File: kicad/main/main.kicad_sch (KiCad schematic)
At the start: 15 parts, among them J3 Conn_01x07_Pin, J4 Conn_01x04_Pin, P1 USB_C_Plug_USB2.0, SW3 SW_Push, SW4 SW_Push, U1 HUSB237

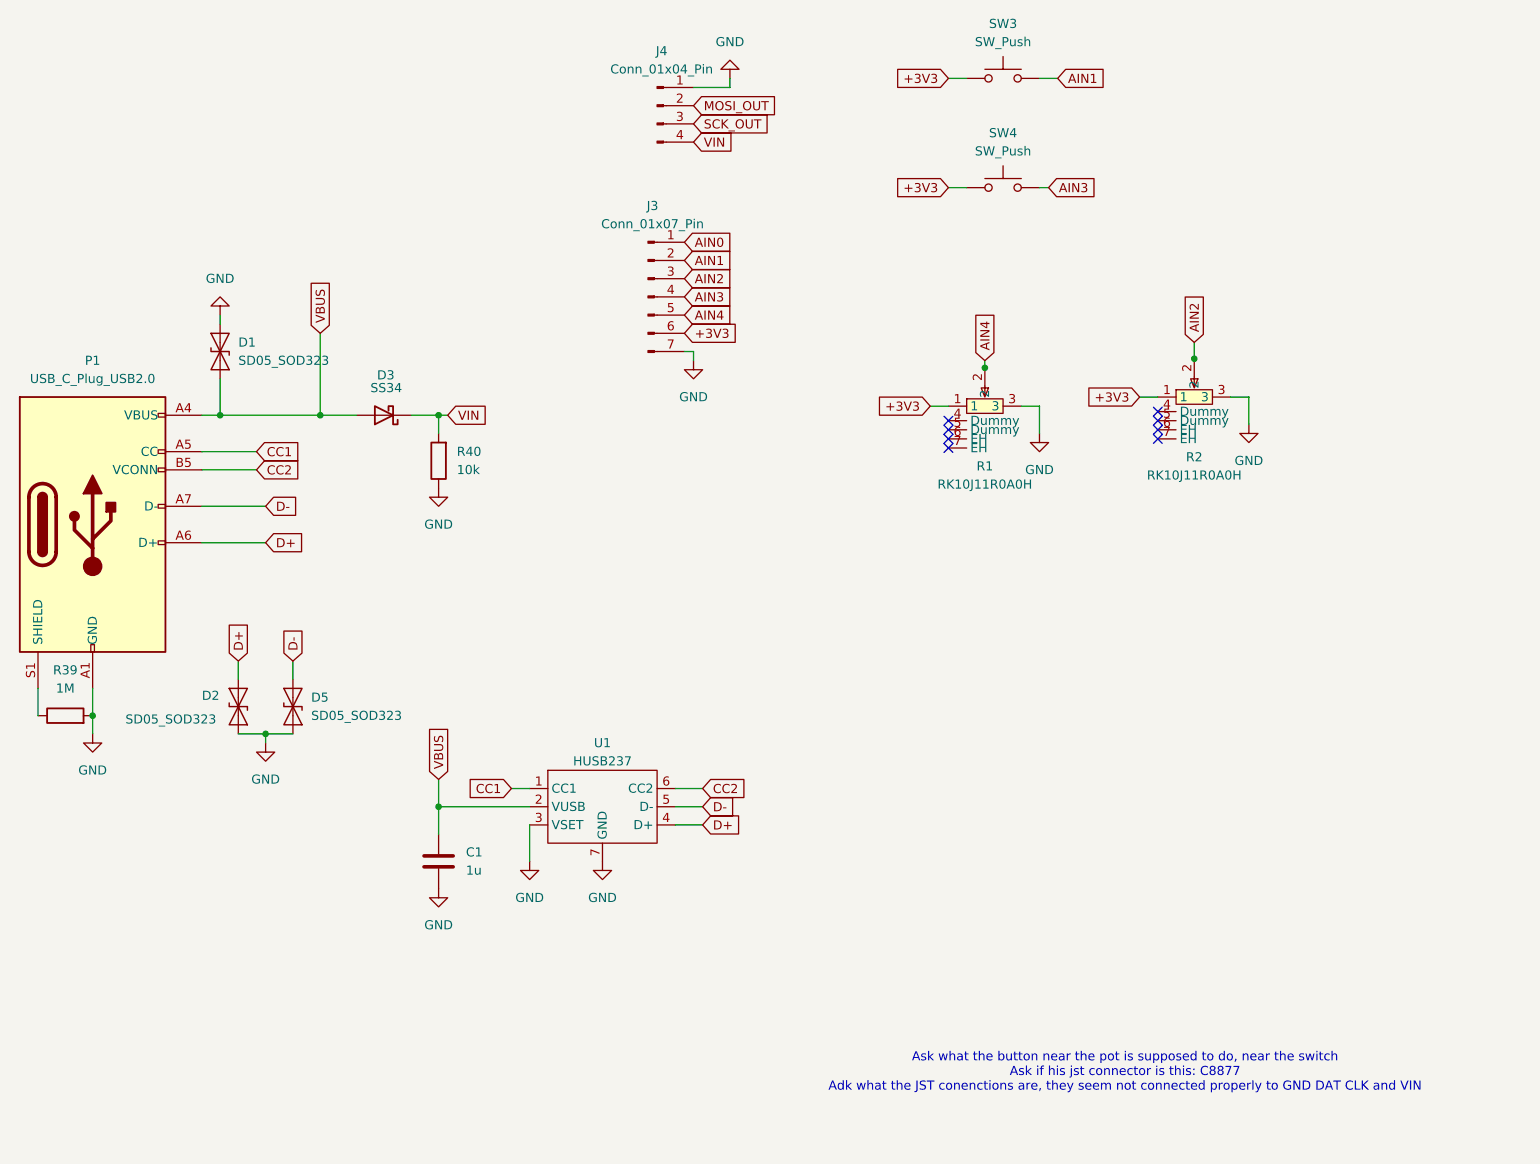
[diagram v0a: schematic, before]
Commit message: Switches added
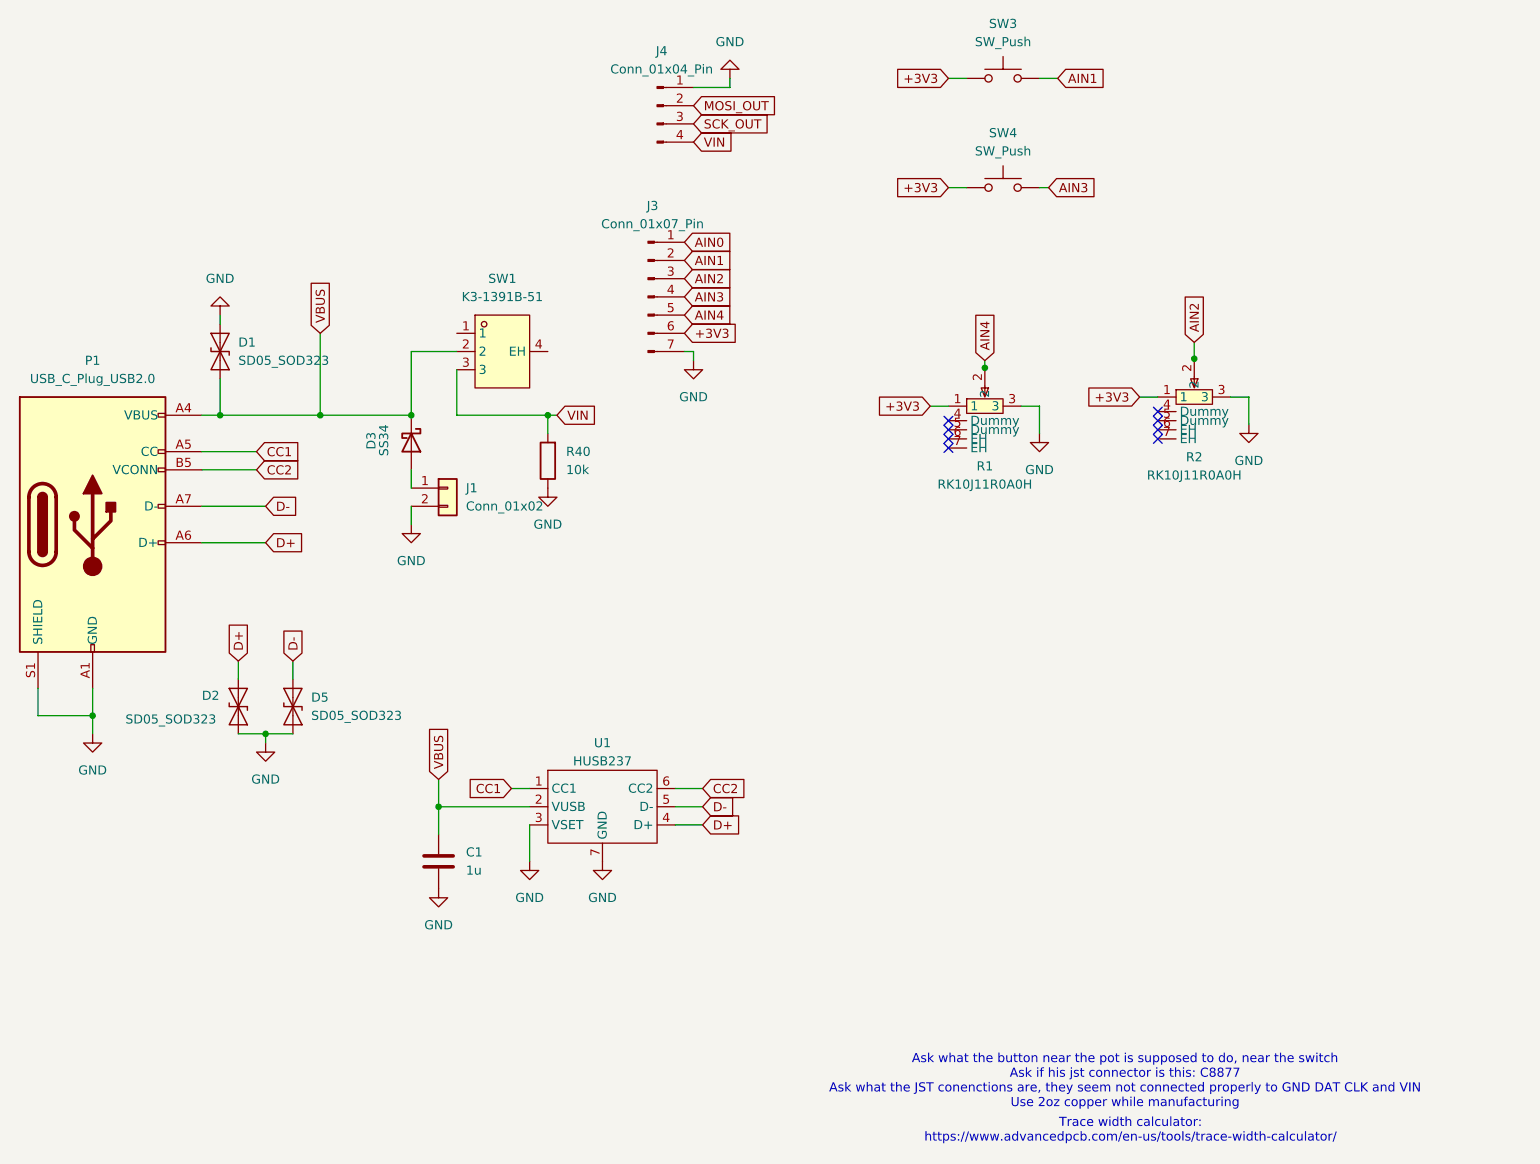
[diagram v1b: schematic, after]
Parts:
- removed R39: 1M, Resistor_SMD:R_0603_1608Metric_Pad0.98x0.95mm_HandSolder, symbol Device:R
- added J1: Conn_01x02, symbol Connector_Generic:Conn_01x02
- added SW1: K3-1391B-51, easyeda2kicad:SW-TH_K3-1391B-51, symbol easyeda2kicad:K3-1391B-51
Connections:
- net GND: now also P1.S1 (SHIELD), J1.2 (Pin_2)
- net VBUS: now also D3.1 (K), SW1.2; no longer D3.2 (A)
- net VIN: now also SW1.3; no longer D3.1 (K)
- new net: D3.2 (A), J1.1 (Pin_1)
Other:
- note added: "Ask what the button near the pot is supposed to do, near the switch Ask if his jst connector is this: C8877 Ask what the JST conenctions are, they seem not connected properly to GND DAT CLK and VIN Use 2oz copper while manufacturing"
- note added: "Trace width calculator: https://www.advancedpcb.com/en-us/tools/trace-width-calculator/"
- note removed: "Ask what the button near the pot is supposed to do, near the switch Ask if his jst connector is this: C8877 Adk what the JST conenctions are, they seem not connected properly to GND DAT CLK and VIN"
- moved on the sheet: D3, R40

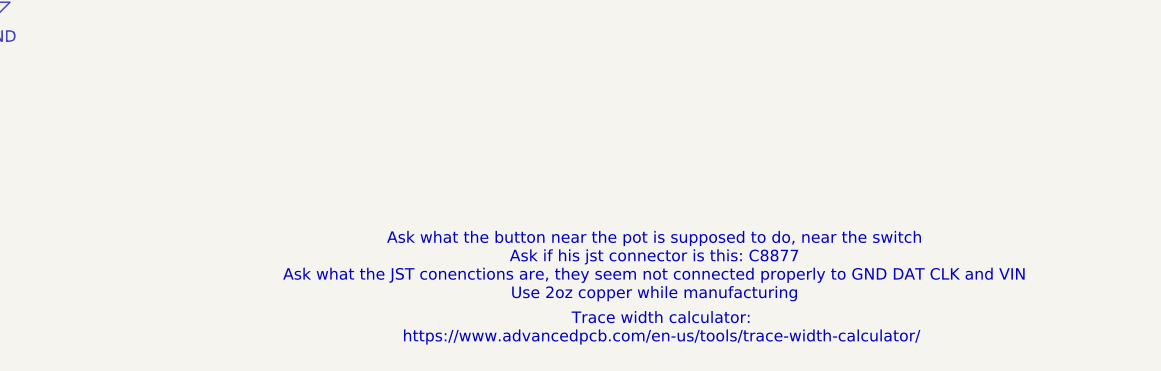
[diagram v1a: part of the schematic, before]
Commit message: Added extra switched
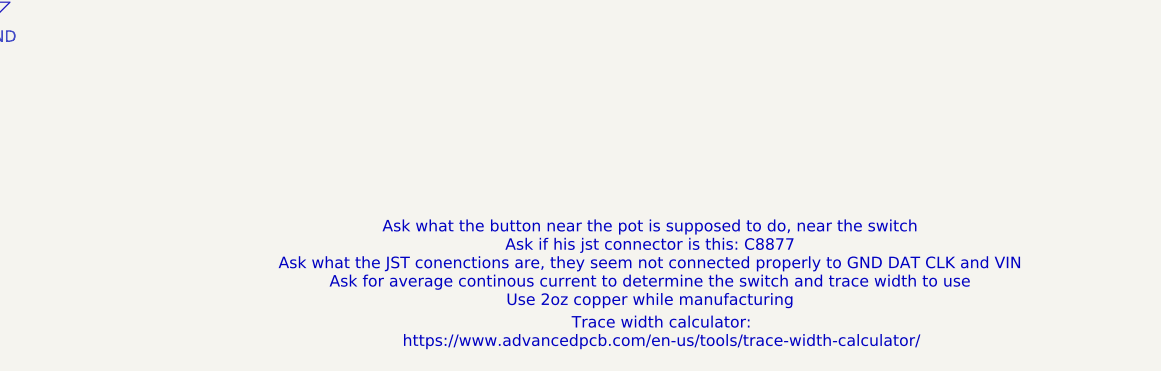
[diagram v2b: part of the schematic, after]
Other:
- note added: "Ask what the button near the pot is supposed to do, near the switch Ask if his jst connector is this: C8877 Ask what the JST conenctions are, they seem not connected properly to GND DAT CLK and VIN Ask for average continous current to determine the switch and trace width to use Use 2oz copper while manufacturing"
- note removed: "Ask what the button near the pot is supposed to do, near the switch Ask if his jst connector is this: C8877 Ask what the JST conenctions are, they seem not connected properly to GND DAT CLK and VIN Use 2oz copper while manufacturing"
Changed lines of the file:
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@@
 	(text "Trace width calculator:\nhttps://www.advancedpcb.com/en-us/tools/trace-width-calculator/"
 		(exclude_from_sim no)
-		(at 231.14 178.562 0)
+		(at 231.14 179.07 0)
 		(effects
 			(font
@@
 		)
 	)
-	(text "Ask what the button near the pot is supposed to do, near the switch\nAsk if his jst connector is this: C8877\nAsk what the JST conenctions are, they seem not connected properly to GND DAT CLK and VIN\nUse 2oz copper while manufacturing"
+	(text "Ask what the button near the pot is supposed to do, near the switch\nAsk if his jst connector is this: C8877\nAsk what the JST conenctions are, they seem not connected properly to GND DAT CLK and VIN\nAsk for average continous current to determine the switch and trace width to use\nUse 2oz copper while manufacturing"
 		(exclude_from_sim yes)
-		(at 230.378 171.704 0)
+		(at 229.87 171.45 0)
 		(effects
 			(font

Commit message: Finished design
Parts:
- removed SW1: K3-1391B-51, easyeda2kicad:SW-TH_K3-1391B-51, symbol easyeda2kicad:K3-1391B-51
- added SW1: MK-12C03-G015, easyeda2kicad:SW-SMD_MK-12C03-G015, symbol easyeda2kicad:MK-12C03-G015
- added U2: ZX-PH2.0-WT4P, easyeda2kicad:CONN-SMD_4P-P2.00_C2001RS10411M0101RC, symbol easyeda2kicad:ZX-PH2.0-WT4P
- C1: footprint (none) -> Capacitor_SMD:C_0805_2012Metric
- J2: renamed from J1; footprint (none) -> Connector_PinHeader_2.54mm:PinHeader_1x02_P2.54mm_Vertical
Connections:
- net GND: now also U2.3, U2.5, U2.6
- net MOSI_OUT: now also U2.2
- net SCK_OUT: now also U2.1
- net VBUS: now also SW1.3
- net VIN: now also SW1.2, U2.4
- no-connect marks 8 -> 13

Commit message: Rewired PCB
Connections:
- net D+: now also D2.1 (A1); no longer D2.2 (A2)
- net D-: now also D5.1 (A1); no longer D5.2 (A2)
- net GND: now also D2.2 (A2), D5.2 (A2); no longer D2.1 (A1), D5.1 (A1)
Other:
- moved on the sheet: C1, D1, D2, D3, D5, J2, J3, J4, P1, R1, R2, R40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

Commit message: Rewired PCB
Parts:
- removed D3: SS34, Diode_SMD:D_SMA, symbol Diode:SS34
- added D3: 1N4007, Diode_THT:D_DO-41_SOD81_P10.16mm_Horizontal, symbol Diode:1N4007
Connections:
- net VBUS: now also D3.1 (K)
- net at J2.1 (Pin_1): now also D3.2 (A)
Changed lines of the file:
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@@
 	)
 	(symbol
-		(lib_id "Diode:SS34")
+		(lib_id "Diode:1N4007")
 		(at 132.08 93.98 270)
 		(unit 1)
@@
 		(on_board yes)
 		(dnp no)
+		(fields_autoplaced yes)
 		(property "Reference" "D3"
-			(at 126.492 93.726 0)
+			(at 134.62 92.7099 90)
 			(effects
 				(font
 					(size 1.27 1.27)
 				)
+				(justify left)
 			)
 		)
-		(property "Value" "SS34"
-			(at 128.27 93.6625 0)
+		(property "Value" "1N4007"
+			(at 134.62 95.2499 90)
 			(effects
 				(font
 					(size 1.27 1.27)
 				)
+				(justify left)
 			)
 		)
-		(property "Footprint" "Diode_SMD:D_SMA"
+		(property "Footprint" "Diode_THT:D_DO-41_SOD81_P10.16mm_Horizontal"
 			(at 127.635 93.98 0)
 			(effects
@@
 			)
 		)
-		(property "Datasheet" "https://www.vishay.com/docs/88751/ss32.pdf"
+		(property "Datasheet" "http://www.vishay.com/docs/88503/1n4001.pdf"
 			(at 132.08 93.98 0)
 			(effects
@@
 			)
 		)
-		(property "Description" "40V 3A Schottky Diode, SMA"
+		(property "Description" "1000V 1A General Purpose Rectifier Diode, DO-41"
 			(at 132.08 93.98 0)
 			(effects
@@
 			)
 		)
-		(property "LCSC Part" "C8678"
+		(property "Sim.Device" "D"
 			(at 132.08 93.98 0)
 			(effects
@@
 			)
 		)
-		(pin "1"
+		(property "Sim.Pins" "1=K 2=A"
+			(at 132.08 93.98 0)
+			(effects
+				(font
+					(size 1.27 1.27)
+				)
+				(hide yes)
+			)
 		)
 		(pin "2"
 		)
+		(pin "1"
+		)
 		(instances

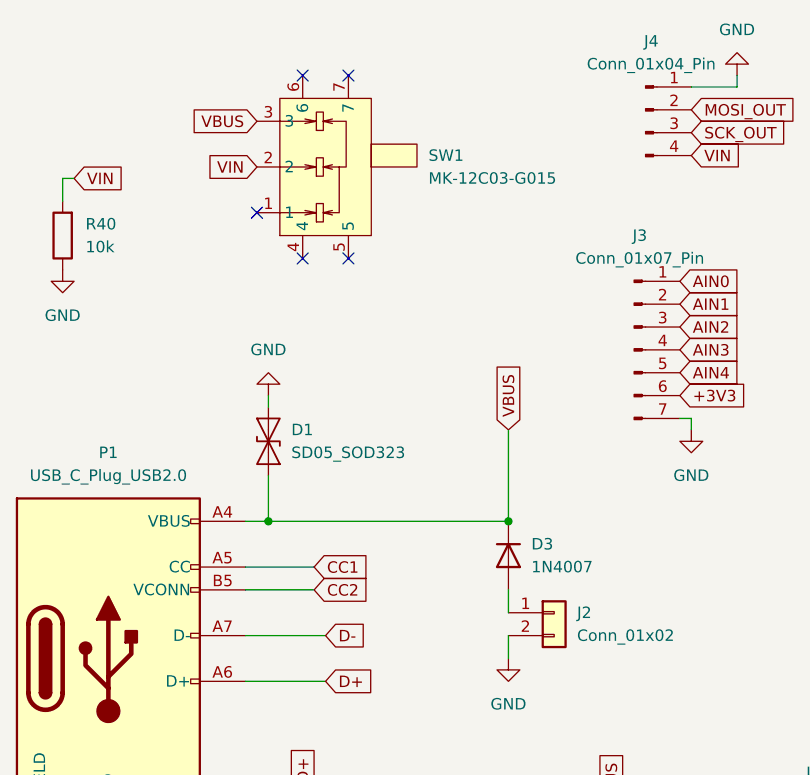
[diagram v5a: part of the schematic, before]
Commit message: Final push with moved components
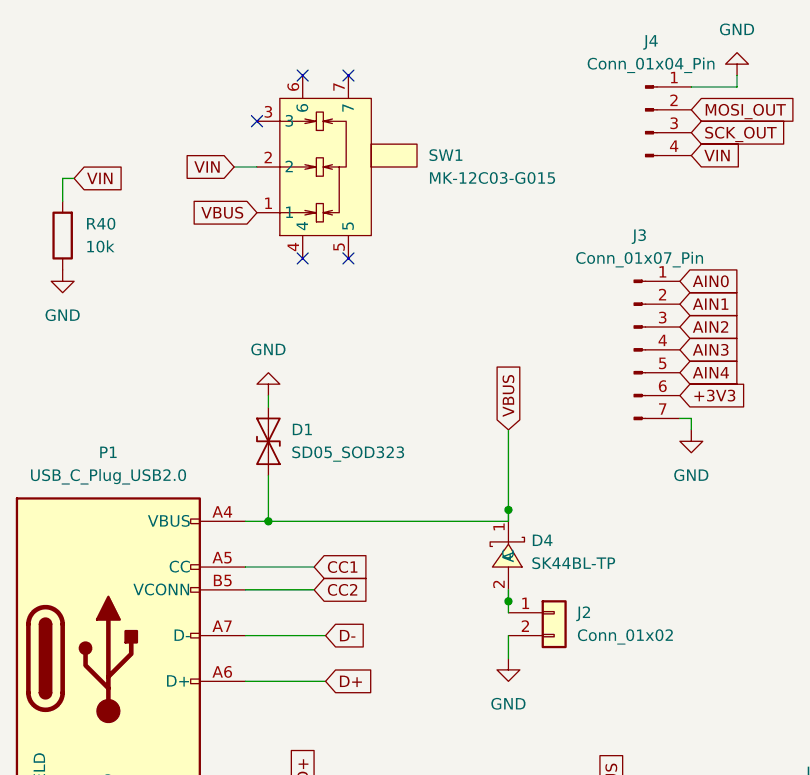
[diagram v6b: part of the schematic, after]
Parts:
- removed D3: 1N4007, Diode_THT:D_DO-41_SOD81_P10.16mm_Horizontal, symbol Diode:1N4007
- added D4: SK44BL-TP, easyeda2kicad:SMB_L4.6-W3.6-LS5.3-RD, symbol easyeda2kicad:SK44BL-TP
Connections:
- net VBUS: now also SW1.1, D4.1 (C); no longer SW1.3
- net at J2.1 (Pin_1): now also D4.2 (A)
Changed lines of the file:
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@@
 	)
 	(junction
-		(at 132.08 90.17)
+		(at 111.76 134.62)
 		(diameter 0)
 		(color 0 0 0 0)
 	)
 	(junction
-		(at 111.76 134.62)
+		(at 132.08 88.9)
 		(diameter 0)
 		(color 0 0 0 0)
@@
 		(color 0 0 0 0)
 	)
+	(junction
+		(at 132.08 99.06)
+		(diameter 0)
+		(color 0 0 0 0)
+	)
 	(no_connect
 		(at 213.36 101.09)
 	)
 	(no_connect
-		(at 104.14 55.88)
+		(at 104.14 45.72)
 	)
 	(no_connect
@@
 	(wire
 		(pts
-			(xy 132.08 97.79) (xy 132.08 100.33)
+			(xy 132.08 97.79) (xy 132.08 99.06)
 		)
 		(stroke
@@
 	(wire
 		(pts
-			(xy 132.08 80.01) (xy 132.08 90.17)
+			(xy 132.08 80.01) (xy 132.08 88.9)
+		)
+		(stroke
+			(width 0)
+			(type default)
+		)
+	)
+	(wire
+		(pts
+			(xy 132.08 99.06) (xy 132.08 100.33)
 		)
 		(stroke
@@
 	(wire
 		(pts
+			(xy 101.6 50.8) (xy 104.14 50.8)
+		)
+		(stroke
+			(width 0)
+			(type default)
+		)
+	)
+	(wire
+		(pts
 			(xy 102.87 107.95) (xy 111.76 107.95)
 		)
@@
 	(wire
 		(pts
+			(xy 132.08 88.9) (xy 132.08 90.17)
+		)
+		(stroke
+			(width 0)
+			(type default)
+		)
+	)
+	(wire
+		(pts
 			(xy 176.53 124.46) (xy 180.34 124.46)
 		)
@@
 	(global_label "VIN"
 		(shape input)
-		(at 104.14 50.8 180)
+		(at 101.6 50.8 180)
 		(fields_autoplaced yes)
 		(effects
@@
 		)
 		(property "Intersheetrefs" "${INTERSHEET_REFS}"
-			(at 98.1309 50.8 0)
+			(at 95.5909 50.8 0)
 			(effects
 				(font
@@
 	(global_label "VBUS"
 		(shape input)
-		(at 104.14 45.72 180)
+		(at 104.14 55.88 180)
 		(fields_autoplaced yes)
 		(effects
@@
 		)
 		(property "Intersheetrefs" "${INTERSHEET_REFS}"
-			(at 96.2562 45.72 0)
+			(at 96.2562 55.88 0)
 			(effects
 				(font
@@
 	)
 	(symbol
-		(lib_id "Diode:1N4007")
-		(at 132.08 93.98 270)
-		(unit 1)
-		(exclude_from_sim no)
-		(in_bom yes)
-		(on_board yes)
-		(dnp no)
-		(fields_autoplaced yes)
-		(property "Reference" "D3"
-			(at 134.62 92.7099 90)
-			(effects
-				(font
-					(size 1.27 1.27)
-				)
-				(justify left)
-			)
-		)
-		(property "Value" "1N4007"
-			(at 134.62 95.2499 90)
-			(effects
-				(font
-					(size 1.27 1.27)
-				)
-				(justify left)
-			)
-		)
-		(property "Footprint" "Diode_THT:D_DO-41_SOD81_P10.16mm_Horizontal"
-			(at 127.635 93.98 0)
-			(effects
-				(font
-					(size 1.27 1.27)
-				)
-				(hide yes)
-			)
-		)
-		(property "Datasheet" "http://www.vishay.com/docs/88503/1n4001.pdf"
-			(at 132.08 93.98 0)
-			(effects
-				(font
-					(size 1.27 1.27)
-				)
-				(hide yes)
-			)
-		)
-		(property "Description" "1000V 1A General Purpose Rectifier Diode, DO-41"
-			(at 132.08 93.98 0)
-			(effects
-				(font
-					(size 1.27 1.27)
-				)
-				(hide yes)
-			)
-		)
-		(property "Sim.Device" "D"
-			(at 132.08 93.98 0)
-			(effects
-				(font
-					(size 1.27 1.27)
-				)
-				(hide yes)
-			)
-		)
-		(property "Sim.Pins" "1=K 2=A"
-			(at 132.08 93.98 0)
-			(effects
-				(font
-					(size 1.27 1.27)
-				)
-				(hide yes)
-			)
-		)
-		(pin "2"
-		)
-		(pin "1"
-		)
-		(instances
-			(project ""
-				(path "/6c52ee88-cda0-4585-8140-5b6439b12637"
-					(reference "D3")
-					(unit 1)
-				)
-			)
-		)
-	)
-	(symbol
 		(lib_id "Device:R")
 		(at 82.55 58.42 180)
@@
 					(unit 1)
 				)
+			)
+		)
+	)
+	(symbol
+		(lib_id "easyeda2kicad:SK44BL-TP")
+		(at 132.08 93.98 270)
+		(unit 1)
+		(exclude_from_sim no)
+		(in_bom yes)
+		(on_board yes)
+		(dnp no)
+		(fields_autoplaced yes)
+		(property "Reference" "D4"
+			(at 134.62 92.3299 90)
+			(effects
+				(font
+					(size 1.27 1.27)
+				)
+				(justify left)
+			)
+		)
+		(property "Value" "SK44BL-TP"
+			(at 134.62 94.8699 90)
+			(effects
+				(font
+					(size 1.27 1.27)
+				)
+				(justify left)
+			)
+		)
+		(property "Footprint" "easyeda2kicad:SMB_L4.6-W3.6-LS5.3-RD"
+			(at 124.46 93.98 0)
+			(effects
+				(font
+					(size 1.27 1.27)
+				)
+				(hide yes)
+			)
+		)
+		(property "Datasheet" "https://lcsc.com/product-detail/Schottky-Barrier-Diodes-SBD_MCC_SK44BL-TP_SK44BL-TP_C151740.html"
+			(at 121.92 93.98 0)
+			(effects
+				(font
+					(size 1.27 1.27)
+				)
+				(hide yes)
+			)
+		)
+		(property "Description" ""
+			(at 132.08 93.98 0)
+			(effects
+				(font
+					(size 1.27 1.27)
+				)
+				(hide yes)
+			)
+		)
+		(property "LCSC Part" "C151740"
+			(at 119.38 93.98 0)
+			(effects
+				(font
+					(size 1.27 1.27)
+				)
+				(hide yes)
+			)
+		)
+		(pin "1"
+		)
+		(pin "2"
+		)
+		(instances
+			(project ""
+				(path "/6c52ee88-cda0-4585-8140-5b6439b12637"
+					(reference "D4")
+					(unit 1)
+				)

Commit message: Revamped PCB
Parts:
- removed R2: RK10J11R0A0H, easyeda2kicad:RES-SMD_RK10J11R0A0H, symbol easyeda2kicad:RK10J11R0A0H
- removed SW1: MK-12C03-G015, easyeda2kicad:SW-SMD_MK-12C03-G015, symbol easyeda2kicad:MK-12C03-G015
- removed U2: ZX-PH2.0-WT4P, easyeda2kicad:CONN-SMD_4P-P2.00_C2001RS10411M0101RC, symbol easyeda2kicad:ZX-PH2.0-WT4P
- added J9: Conn_01x02, symbol Connector_Generic:Conn_01x02
- added SW2: MK-12D18-G040, easyeda2kicad:SW-TH_MK-12D18-G040, symbol easyeda2kicad:MK-12D18-G040
- added U3: S4B-XH-SM4-TB-(LF)(SN), easyeda2kicad:CONN-SMD_S4B-XH-SM4-TB-LF-SN, symbol easyeda2kicad:S4B-XH-SM4-TB-(LF)(SN)
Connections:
- net AIN1: now also J3.3 (Pin_3), J9.1 (Pin_1); no longer J3.2 (Pin_2)
- net AIN2: now also J3.2 (Pin_2); no longer J3.3 (Pin_3)
- net AIN3: now also J9.2 (Pin_2)
- net GND: now also U3.1
- net MOSI_OUT: now also U3.2
- net SCK_OUT: now also U3.3
- net VBUS: now also SW2.1
- net VIN: now also SW2.2, U3.4, U3.5, U3.6
- no-connect marks 13 -> 9
